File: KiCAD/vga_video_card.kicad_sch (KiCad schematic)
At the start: 16 parts, among them J1 DE15_Socket_HighDensity, J6 Conn_02x20_Odd_Even, SW1 rst_btn, SW2 SW_DPDT_x2, SW3 SW_DPDT_x2, SW4 SW_DPDT_x2, U27 74HC04, U39 74HC02, Y1 10MHz

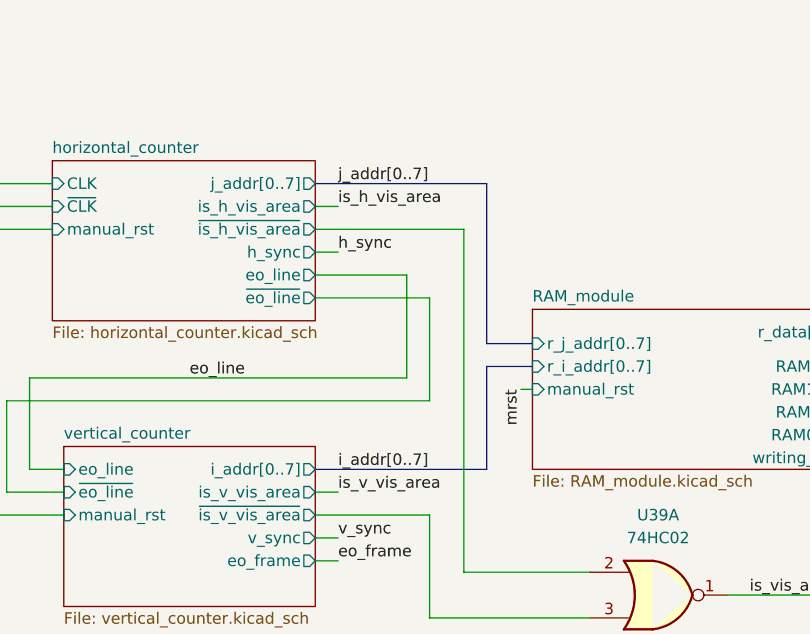
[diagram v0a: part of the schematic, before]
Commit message: resolved most ERC errors
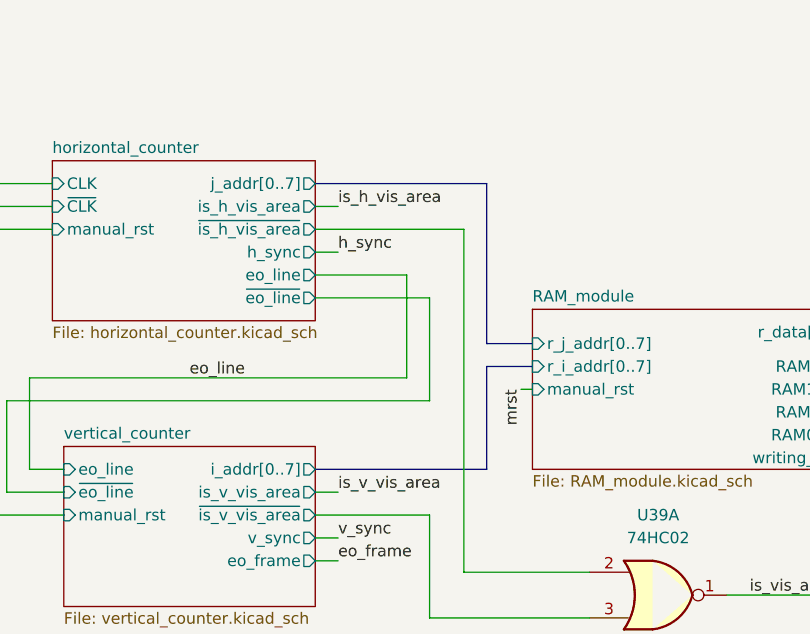
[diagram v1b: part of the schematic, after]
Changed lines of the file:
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@@
-		)
-	)
-	(label "i_addr[0..7]"
-		(at 134.62 73.66 0)
-		(effects
-			(font
-				(size 1.27 1.27)
-			)
-			(justify left bottom)
 		)
 	)
@@
 		)
 	)
-	(label "j_addr[0..7]"
-		(at 134.62 41.91 0)
-		(effects
-			(font
-				(size 1.27 1.27)
-			)
-			(justify left bottom)
-		)
-	)

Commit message: partially finished pcb layout
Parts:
- added SW5: SW_Slide_DPDT, symbol Switch:SW_Slide_DPDT
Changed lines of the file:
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@@
+	)
+	(symbol
+		(lib_id "Switch:SW_Slide_DPDT")
+		(at 110.49 114.3 0)
+		(unit 1)
+		(exclude_from_sim no)
+		(in_bom yes)
+		(on_board yes)
+		(dnp no)
+		(fields_autoplaced yes)
+		(property "Reference" "SW5"
+			(at 110.49 104.14 0)
+			(effects
+				(font
+					(size 1.27 1.27)
+				)
+			)
+		)
+		(property "Value" "SW_Slide_DPDT"
+			(at 110.49 106.68 0)
+			(effects
+				(font
+					(size 1.27 1.27)
+				)
+			)
+		)
+		(property "Footprint" ""
+			(at 124.46 109.22 0)
+			(effects
+				(font
+					(size 1.27 1.27)
+				)
+				(hide yes)
+			)
+		)
+		(property "Datasheet" "~"
+			(at 110.49 114.3 0)
+			(effects
+				(font
+					(size 1.27 1.27)
+				)
+				(hide yes)
+			)
+		)
+		(property "Description" "Slide Switch, dual pole double throw"
+			(at 110.49 114.3 0)
+			(effects
+				(font
+					(size 1.27 1.27)
+				)
+				(hide yes)
+			)
+		)
+		(pin "4"
+		)
+		(pin "5"
+		)
+		(pin "6"
+		)
+		(pin "1"
+		)
+		(pin "2"
+		)
+		(pin "3"
+		)
+		(instances
+			(project ""
+				(path "/53ebbfbe-eaa1-4706-acc1-611a99db7179"
+					(reference "SW5")
+					(unit 1)
+				)
+			)
+		)
 	)
 	(symbol

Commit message: finished layout
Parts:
- removed SW2, SW3, SW4: SW_DPDT_x2, Button_Switch_THT:SW_CK_JS202011CQN_DPDT_Straight, symbol Switch:SW_DPDT_x2
- added SW3, SW4: SW_Slide_DPDT, Button_Switch_THT:SW_CK_JS202011CQN_DPDT_Straight, symbol Switch:SW_Slide_DPDT
- SW2: renamed from SW5; footprint (none) -> Button_Switch_THT:SW_CK_JS202011CQN_DPDT_Straight
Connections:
- net ext_B: now also SW4.3 (C), SW4.4 (A)
- net ext_G: now also SW3.3 (C), SW3.4 (A)
- net ext_R: now also SW2.3 (C), SW2.4 (A)
- net int_brightness: now also SW2.1 (A), SW2.6 (C), SW3.1 (A), SW3.6 (C), SW4.1 (A), SW4.6 (C)
- net at RV2.2: now also SW2.2 (B), SW2.5 (B)
- net at RV4.2: now also SW4.2 (B), SW4.5 (B)
- net at RV3.2: now also SW3.2 (B), SW3.5 (B)
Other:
- moved on the sheet: SW2

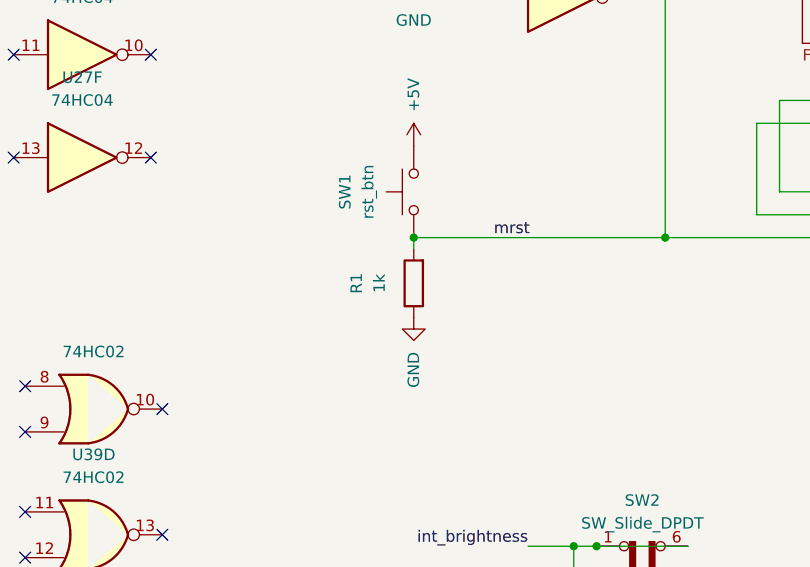
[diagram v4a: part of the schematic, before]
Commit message: update DAC schematics; update pin layout for esp32 connector; update RAM state controller input pin
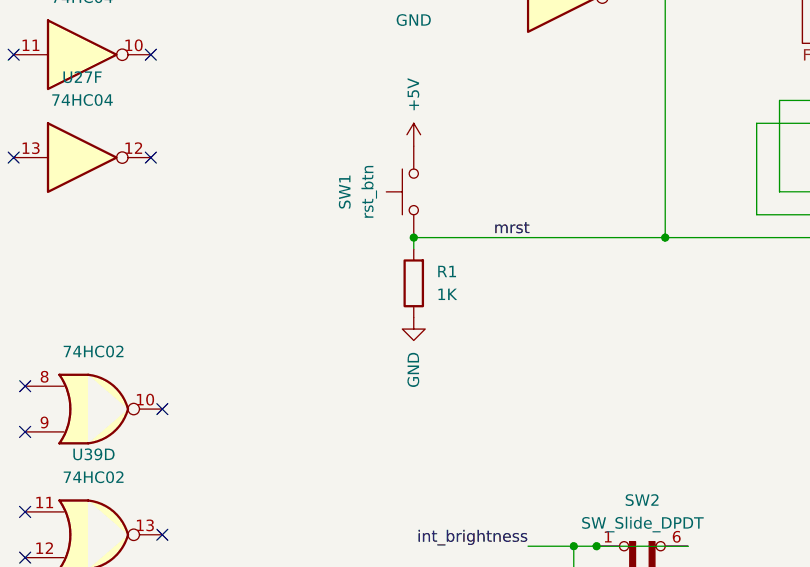
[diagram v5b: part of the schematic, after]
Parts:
- R1: value 1k -> 1K
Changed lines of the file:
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@@
 		(fields_autoplaced yes)
 		(property "Reference" "R1"
-			(at 53.34 83.82 90)
+			(at 62.23 82.5499 0)
 			(effects
 				(font
 					(size 1.27 1.27)
 				)
+				(justify right)
 			)
 		)
-		(property "Value" "1k"
-			(at 55.88 83.82 90)
+		(property "Value" "1K"
+			(at 62.23 85.0899 0)
 			(effects
 				(font
 					(size 1.27 1.27)
 				)
+				(justify right)
 			)
 		)

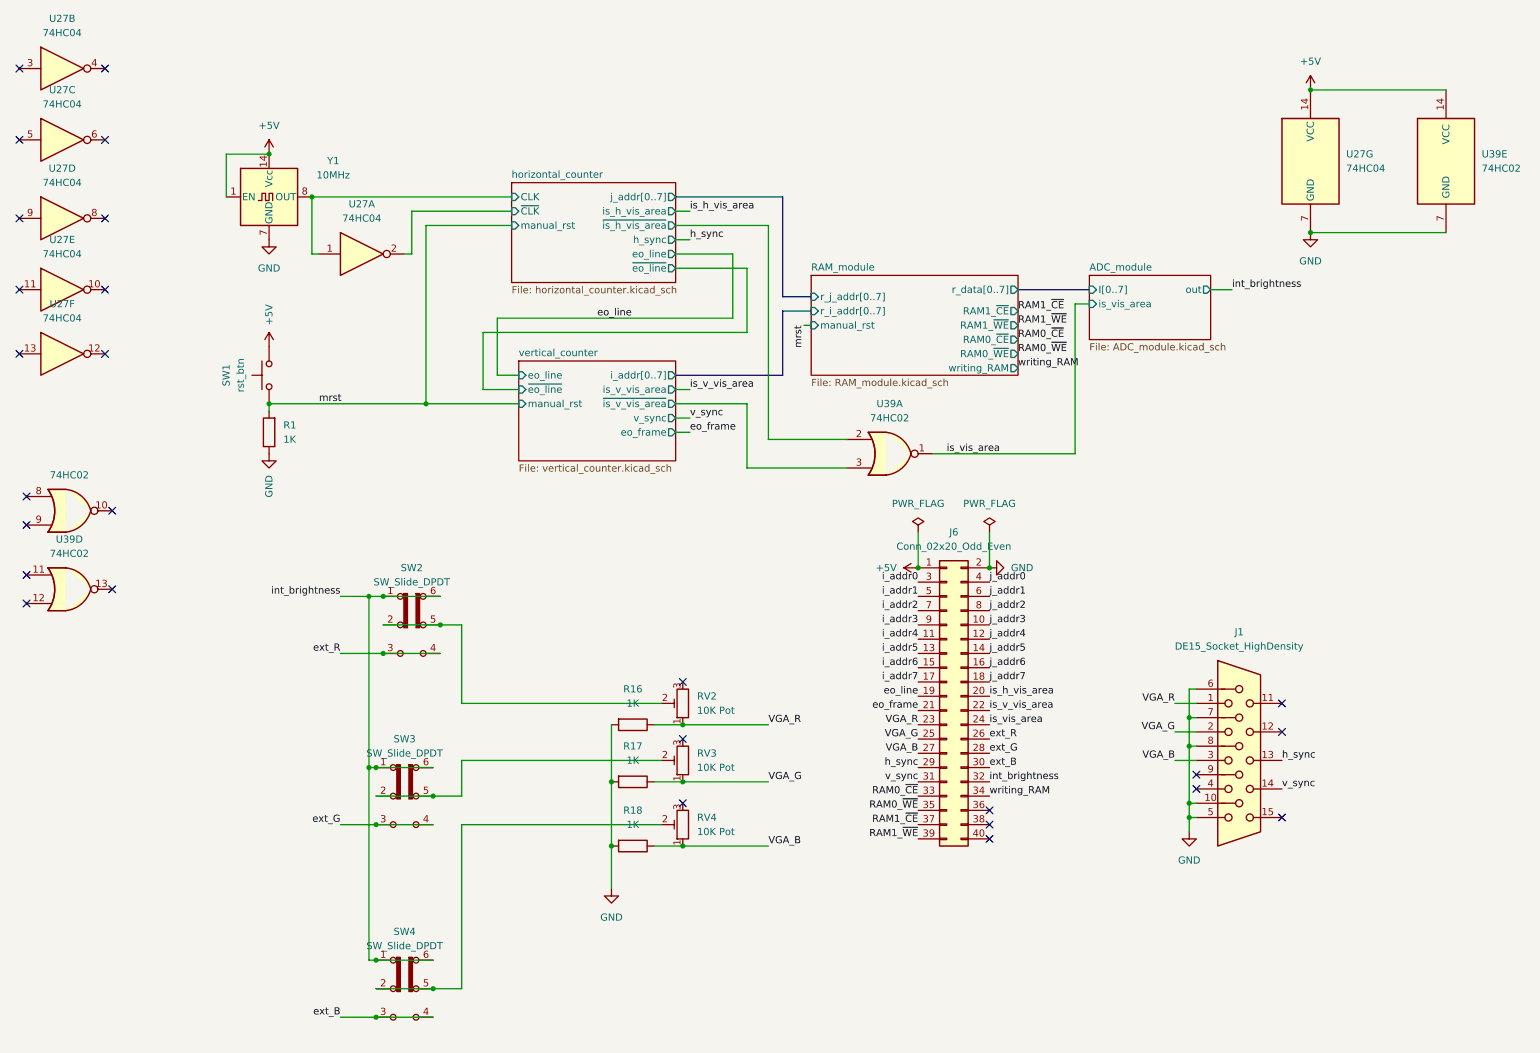
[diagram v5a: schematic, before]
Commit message: passed DRC for PCB
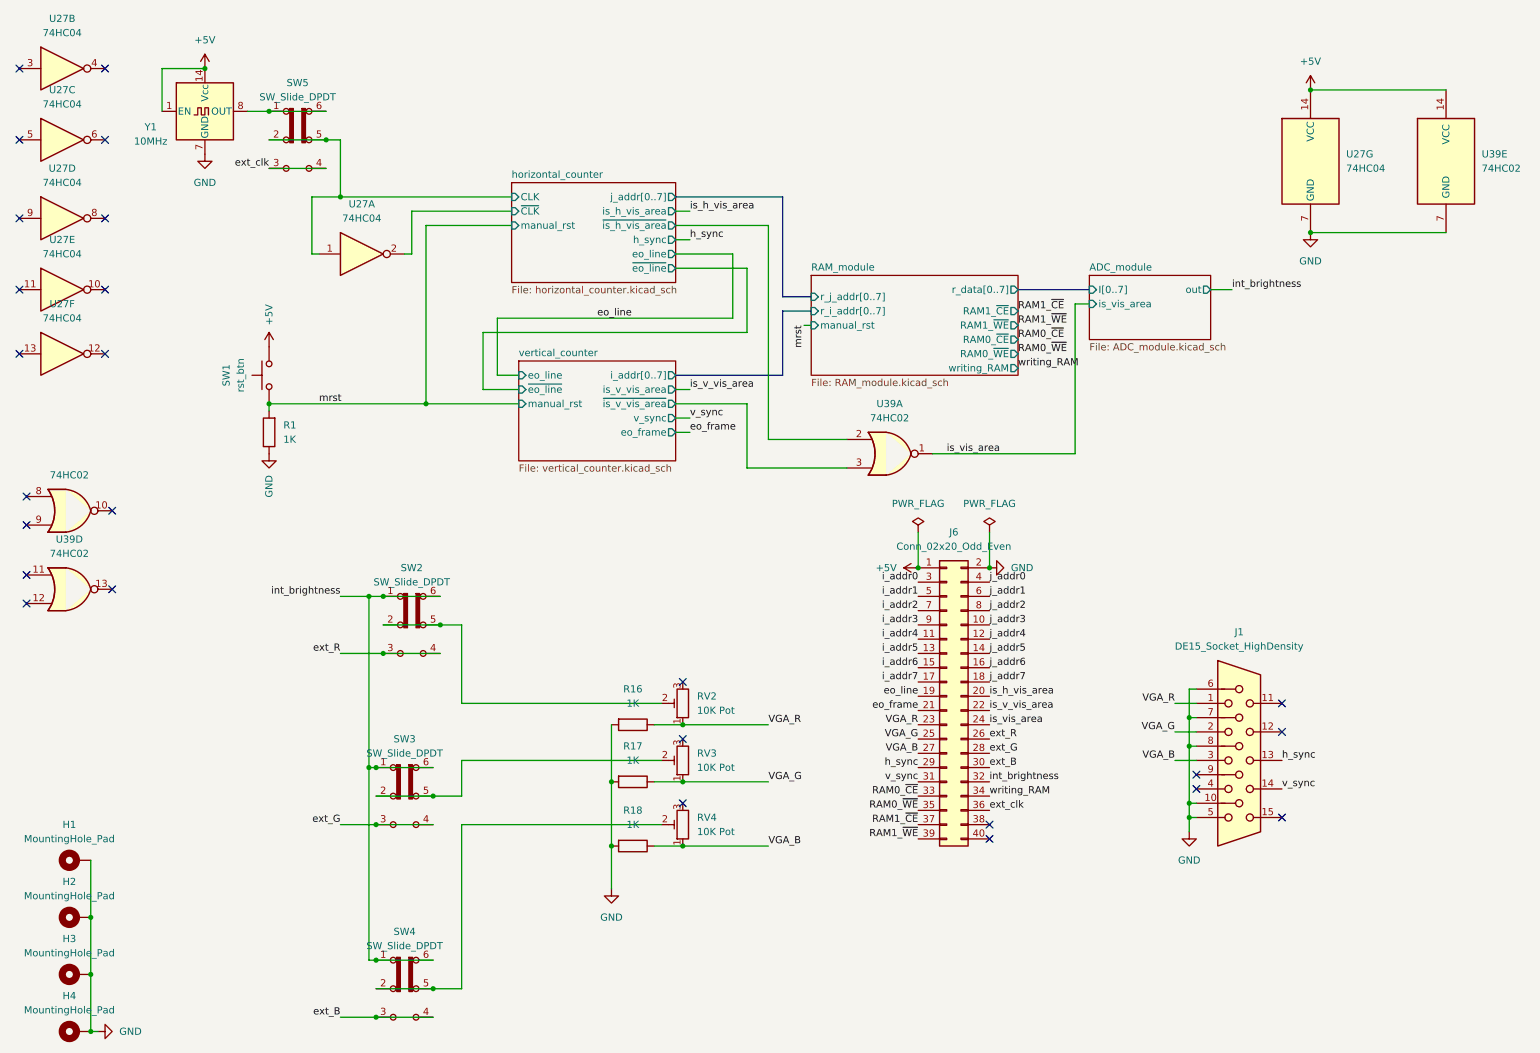
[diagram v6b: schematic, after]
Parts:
- added H1, H2, H3, H4: MountingHole_Pad, MountingHole:MountingHole_3.2mm_M3_Pad_Via, symbol Mechanical:MountingHole_Pad
- added SW5: SW_Slide_DPDT, Button_Switch_THT:SW_CK_JS202011CQN_DPDT_Straight, symbol Switch:SW_Slide_DPDT
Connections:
- net GND: now also H1.1, H2.1, H3.1, H4.1
- net horizontal_counter/CLK: now also SW5.2 (B), SW5.5 (B); no longer Y1.8 (OUT)
- net ext_clk: now reaches J6.36 (Pin_36)
- net ext_clk: now also SW5.3 (C), SW5.4 (A)
- new net: SW5.1 (A), SW5.6 (C), Y1.8 (OUT)
- no-connect marks 27 -> 26
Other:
- moved on the sheet: Y1
